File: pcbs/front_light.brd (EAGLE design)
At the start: 28 x 35 mm, 13 parts, among them IC1 MC34063AD, J1 22-27-2041-04

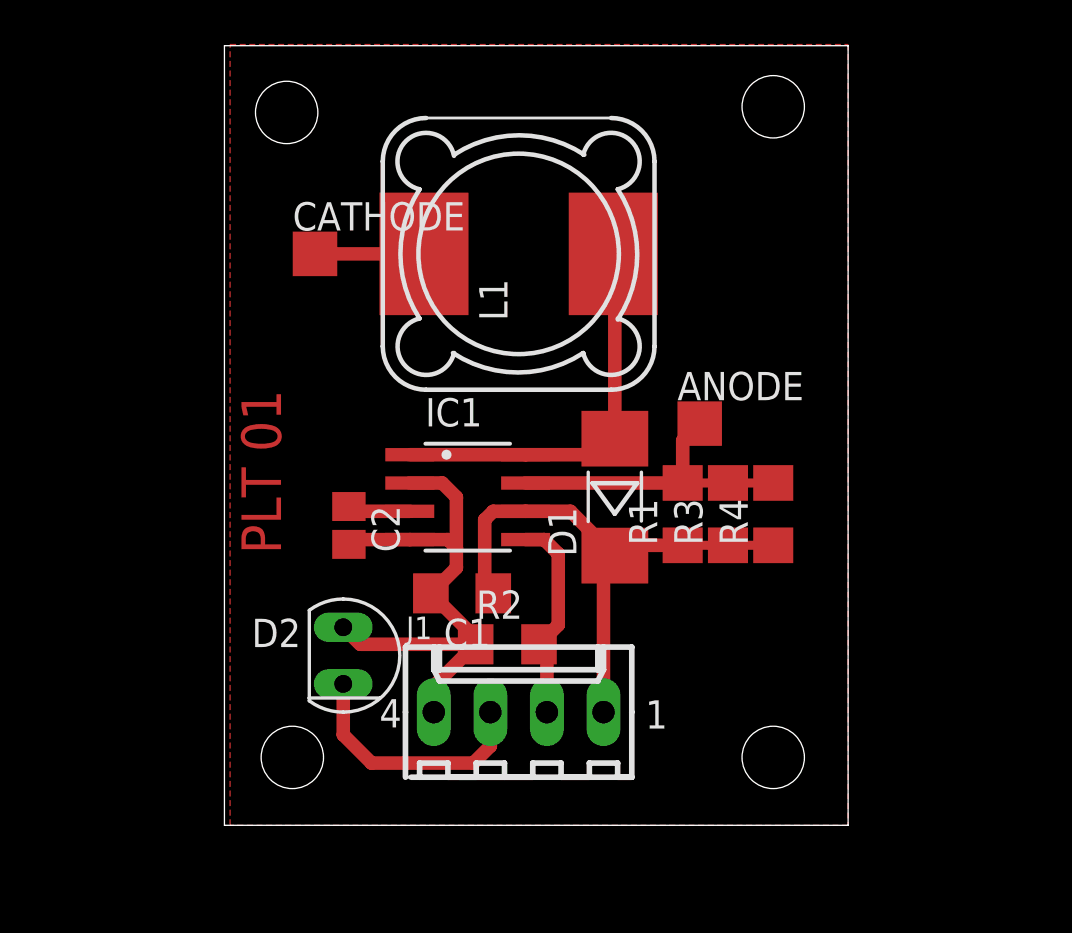
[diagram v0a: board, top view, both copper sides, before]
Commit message: Front light: use attiny and LT3474
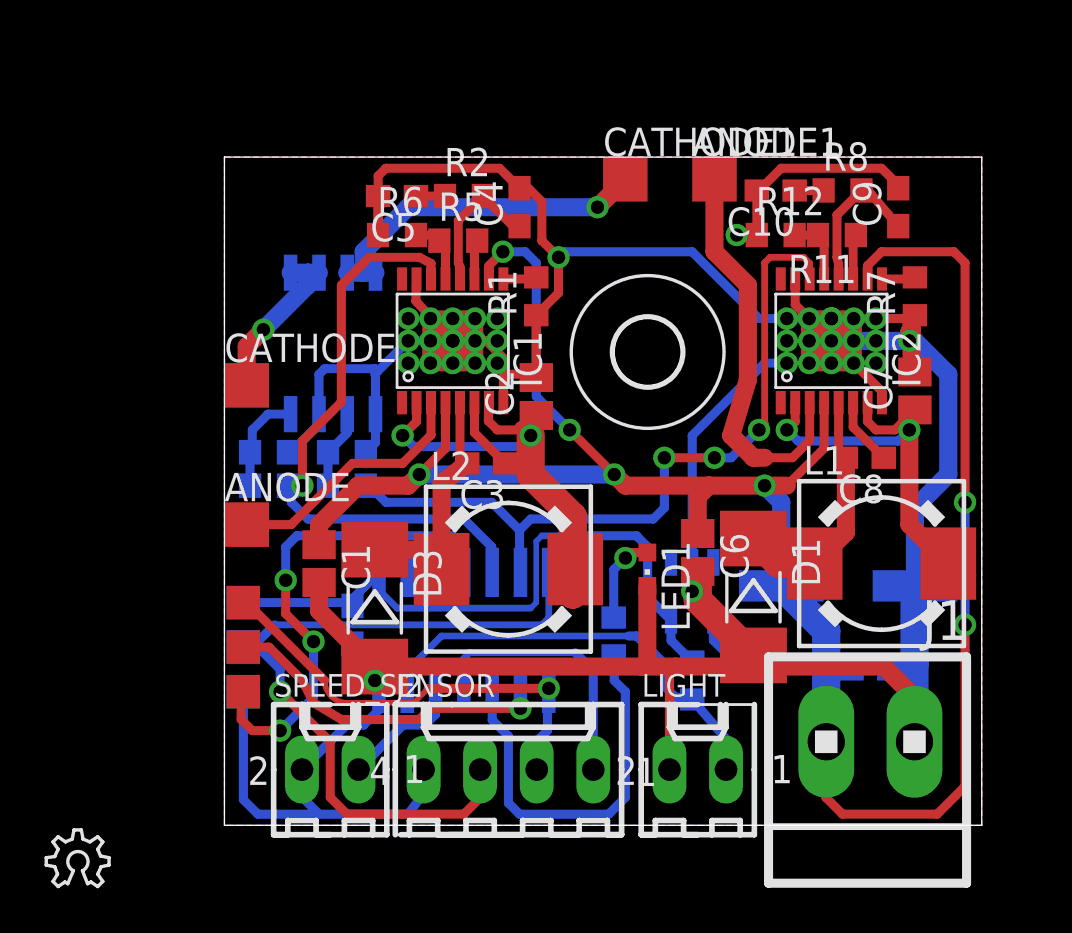
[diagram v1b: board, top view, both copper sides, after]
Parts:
- removed D2: SFH206, opto-trans-siemens:SFH206
- added ANODE1, CATHODE1: TPTP20SQ, testpad:TP20SQ
- added C10, C11, C14, C5: 100n, resistor:C0603
- added C13: 100u, resistor:PANASONIC_E
- added C3, C8: 220n, resistor:C0603
- added C4, C9: 3.3n, resistor:C0603
- added C6, C7: 2.2u, resistor:C0805
- added D3: LL5819, Brunner:MELF-MLL41
- added H1: MOUNT-HOLE3.0, holes:3,0
- added IC2: LT3474, ltc_swr:TSSOP16_BA
- added IC3: ATTINY24/44/84-SSU, attiny24_44_84:SOIC14
- added J2: 22-27-2041-04, con-molex:6410-04
- added L2: DR74, inductors:DR74
- added LED1: (no value), led:CHIPLED_0603
- added LIGHT, SPEED_SENSOR: 22-27-2021-02, con-molex:6410-02
- added LOGO1: OSHW_LOGO_6MILX0100-NT, ea:OSHW_6X100_NOTEXT
- added R10: 100k, resistor:R0603
- added R11, R5: 10k, resistor:R0603
- added R12, R6: 20k, resistor:R0603
- added R13, R14: (no value), resistor:R0603
- added R7, R8: 52.3k, resistor:R0603
- added R9: 33, resistor:R0603
- added U$1: TPS71530, ShortCircuitRobotics:SOT23-DBV
- added U$2: ISP_SPECIALS, bookla:ISP_RM2_00_STRAIGHT
- added U$4: IRF7103, irf-2:SO8-2
- C1: value 10u -> 2.2u; device resistor:C1206 -> resistor:C0805
- C2: value 330p -> 2.2u
- IC1: value MC34063AD -> LT3474; device v-reg-3:SO08 -> ltc_swr:TSSOP16_BA
- J1: value 22-27-2041-04 -> (none); device con-molex:6410-04 -> con-amp:1X2MTA
- L1: value 470u -> DR74; device inductor-coilcraft:MSS1260 -> inductors:DR74
- R1: value 1R0 -> 52.3k; device rcl:R1206 -> resistor:R0603
- R2: value (none) -> 52.3k; device resistor:R1206 -> resistor:R0603
- R3: value 1R0 -> 33; device rcl:R1206 -> resistor:R0603
- R4: value 1R0 -> 100k; device rcl:R1206 -> resistor:R0603
- moved R4 22.8 mm to (2.00, 16.8), flipped to the bottom, turned to 0 degrees
- moved L1 21.4 mm to (29.5, 11.8), turned to 0 degrees
- moved ANODE 20.8 mm to (1.00, 13.5)
- moved R3 20.6 mm to (2.00, 15.2), flipped to the bottom, turned to 0 degrees
- moved R2 20.2 mm to (10.8, 28.2)
- moved J1 15.8 mm to (29.0, 3.75), turned to 180 degrees
- moved R1 11.8 mm to (14.0, 23.8)
- moved C2 10.2 mm to (14.0, 19.2), turned to 90 degrees
- moved D1 7.67 mm to (23.8, 10.2), turned to 270 degrees
- moved IC1 7.05 mm to (10.2, 21.8), turned to 0 degrees
- moved CATHODE 6.65 mm to (1.00, 19.8)
- moved C1 6.56 mm to (4.25, 11.8), turned to 270 degrees
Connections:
- removed net LED_A: ANODE.TP, IC1.7, R1.2, R3.2, R4.2
- removed net LED_C: CATHODE.TP, L1.P$1
- removed net LIGHT: D2.K, J1.3
- removed net PWM: IC1.5, J1.2, R2.2
- new net +12V: C1.1, C11.1, C13.+, C6.1, IC1.10, IC1.4, IC2.10, IC2.4, J1.1, U$1.4
- new net DI: IC3.7, J2.3, U$2.MOSI
- new net DO: IC3.8, J2.2, U$2.RESET
- new net N$10: R3.2, R4.2, U$4.4
- new net N$11: IC1.13, R5.1, R6.2
- new net N$12: C8.2, D1.C, IC2.5, L1.1
- new net N$13: C7.1, IC2.2, IC2.7, L1.2
- new net N$14: IC2.9, R7.2
- new net N$15: IC2.11, R11.1
- new net N$16: C8.1, IC2.6
- new net N$17: C9.1, IC2.12, R8.2
- new net N$18: C10.1, R8.1
- new net N$19: ANODE1.TP, IC2.3
- new net N$2: C2.1, IC1.2, IC1.7, L2.2
- new net N$20: CATHODE1.TP, U$4.7, U$4.8
- new net N$21: R10.2, R9.2, U$4.2
- new net N$22: IC2.13, R11.2, R12.2
- new net N$23: IC3.9, U$2.SCK
- new net N$24: IC3.13, LIGHT.1, R14.1
- new net N$25: IC3.10, R13.1
- new net N$26: LED1.A, R13.2
- new net N$27: IC3.12, SPEED_SENSOR.1
- new net N$3: IC1.11, R5.2
- new net N$4: IC1.9, R1.2
- new net N$5: C3.1, IC1.6
- new net N$6: C4.1, IC1.12, R2.2
- new net N$8: ANODE.TP, IC1.3
- new net N$9: CATHODE.TP, U$4.5, U$4.6
- new net PWM_BIG_LED: IC2.14, IC3.6, R9.1
- new net PWM_DLR: IC1.14, IC3.5, R3.1
- new net RESET: IC3.4, U$2.MISO
- new net WAKE_UP: IC3.11, J2.1
- net GND: now also C10.2, C11.2, C13.-, C14.2, C4.2, C5.2, C6.2, C7.2, C9.2, D1.A, D3.A, IC1.15, IC1.8, IC1.EXP, IC2.15, IC2.8, IC2.EXP, IC3.14, J1.2, J2.4, LED1.C, LIGHT.2, R1.1, R10.1, R12.1, R4.1, R6.1, R7.1, SPEED_SENSOR.2, U$1.2, U$2.VCC, U$4.1, U$4.3; no longer D2.A, IC1.2, IC1.4, J1.4, R2.1
- net N$1: now also C3.2, D3.C, IC1.5, L2.1; no longer D1.A, IC1.1, IC1.8, L1.P$2
- net N$7: now also C5.1, R2.1; no longer C2.1, IC1.3
- net VCC: now also C14.1, IC3.1, R14.2, U$1.5, U$2.GND; no longer C1.1, D1.C, IC1.6, J1.1, R1.1, R3.1, R4.1
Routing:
- net GND: track 25.4 -> 200.2 mm, vias 0 -> 37
- net +12V: track 0.00 -> 108.0 mm, vias 0 -> 7
- net PWM_BIG_LED: track 0.00 -> 34.1 mm, vias 0 -> 3
- net DI: track 0.00 -> 33.2 mm, vias 0 -> 1
- net PWM_DLR: track 0.00 -> 27.5 mm, vias 0 -> 1
- net RESET: track 0.00 -> 22.2 mm, vias 0 -> 3
- net N$2: track 0.00 -> 21.6 mm, vias 0 -> 2
- net DO: track 0.00 -> 20.1 mm, vias 0 -> 1
- net N$24: track 0.00 -> 19.7 mm
- net N$13: track 0.00 -> 18.5 mm, vias 0 -> 2
- net N$19: track 0.00 -> 18.2 mm
- net N$25: track 0.00 -> 17.8 mm
- net N$20: track 0.00 -> 15.3 mm, vias 0 -> 1
- net N$23: track 0.00 -> 15.0 mm, vias 0 -> 1
- net LED_A: track 14.1 -> 0.00 mm
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- added copper zone on layer 16, net GND
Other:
- board size 28 x 35 mm -> 34 x 30 mm
- board text removed: "PLT 01"

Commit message: ForntLight: improved silkscreen
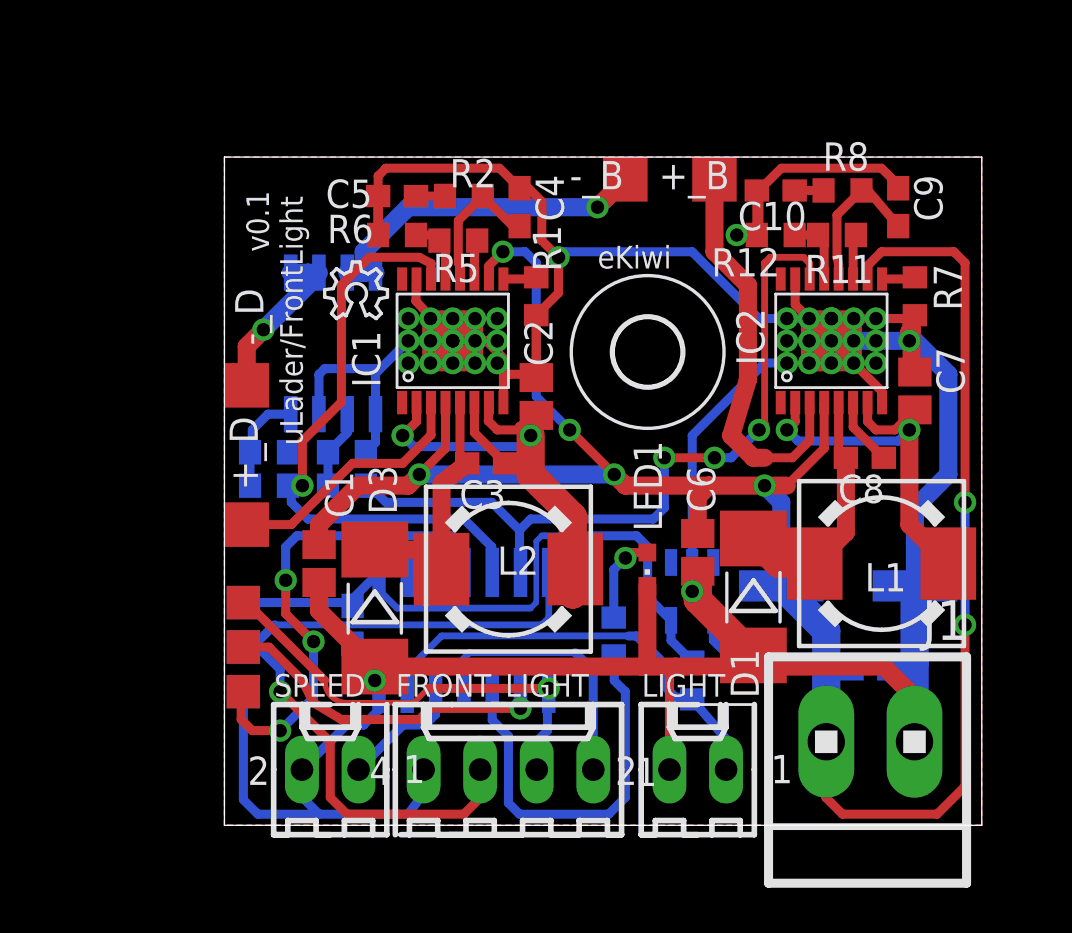
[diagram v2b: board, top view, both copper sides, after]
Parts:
- added LOGO2: OSHW_LOGO_10MILX0350-NT, ea:OSHW_10X350_NOTEXT
- moved LOGO1 28.4 mm to (4.50, 22.8)
- renumbered ANODE to +_D, ANODE1 to +_B, CATHODE to -_D, CATHODE1 to -_B, J2 to FRONT_LIGHT, SPEED_SENSOR to SPEED, U$4 to IRF7103
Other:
- board text added: "eKiwi"
- board text added: "https://github.com/ekiwi/ulader"
- board text added: "https://github.com/roboterclubaachen/xpcc"
- board text added: "uLader/FrontLight"
- board text added: "v0.1"

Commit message: FrontLight: solved some DRC errors
If the .dru file from OSH Park is used
and clearance od same signal smd, pad and via
is set to 0, we do not get any DRC errors.
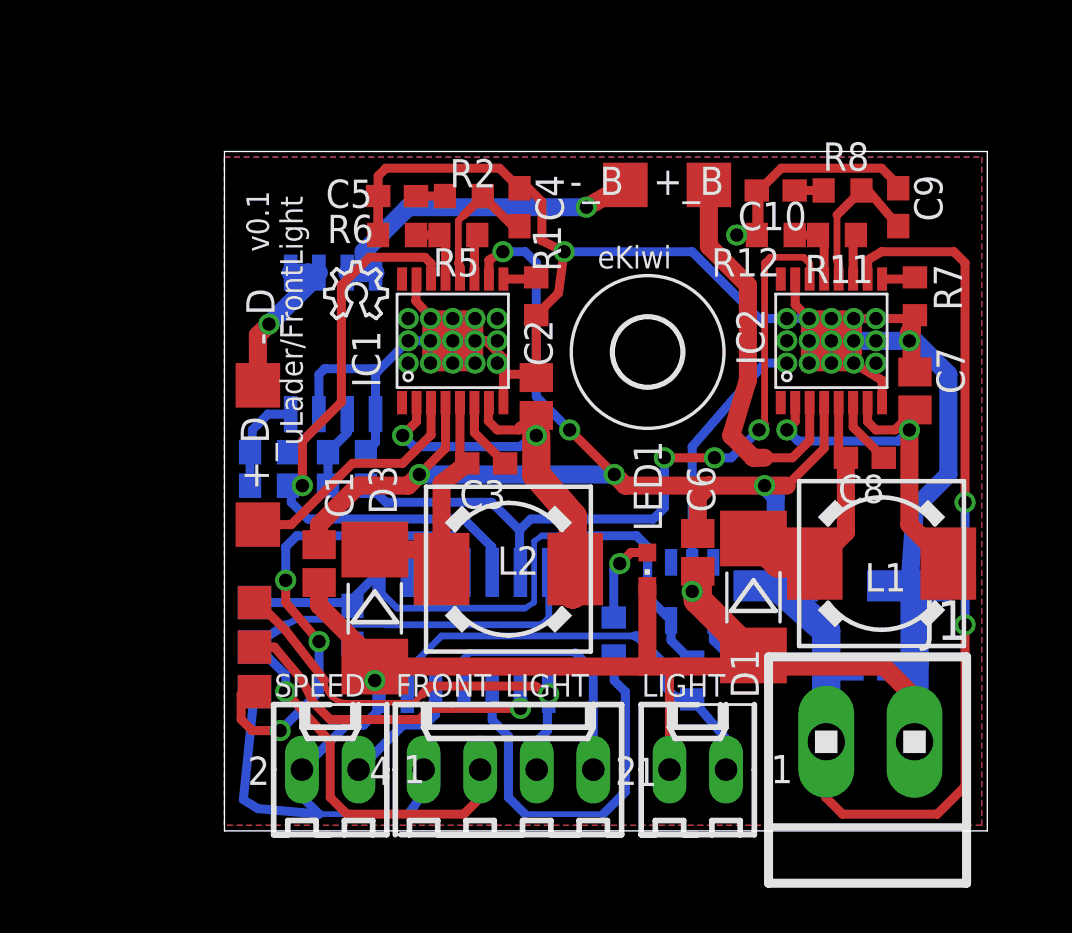
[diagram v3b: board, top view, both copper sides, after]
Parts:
- moved +_D 0.50 mm to (1.50, 13.5)
- moved -_D 0.50 mm to (1.50, 19.8)
- moved U$2 0.50 mm to (0.50, 8.00)
- moved +_B 0.35 mm to (21.8, 28.8)
- moved -_B 0.25 mm to (18.0, 28.8)
- moved C13 0.25 mm to (27.8, 10.8)
- moved R5 0.25 mm to (10.5, 26.5)
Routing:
- net RESET: track 22.2 -> 22.8 mm
- net DO: track 20.1 -> 20.7 mm
- net VCC: track 29.3 -> 28.7 mm
- net N$8: track 11.4 -> 10.9 mm
- net GND: track 200.2 -> 200.4 mm, vias 37 -> 35
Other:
- board size 34 x 30 mm -> 34.2 x 30.5 mm

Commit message: FrontLight: use only one LT3474
Since the DLR and the big led will never be used
together they can be driven by a single
led constant current switching IC.
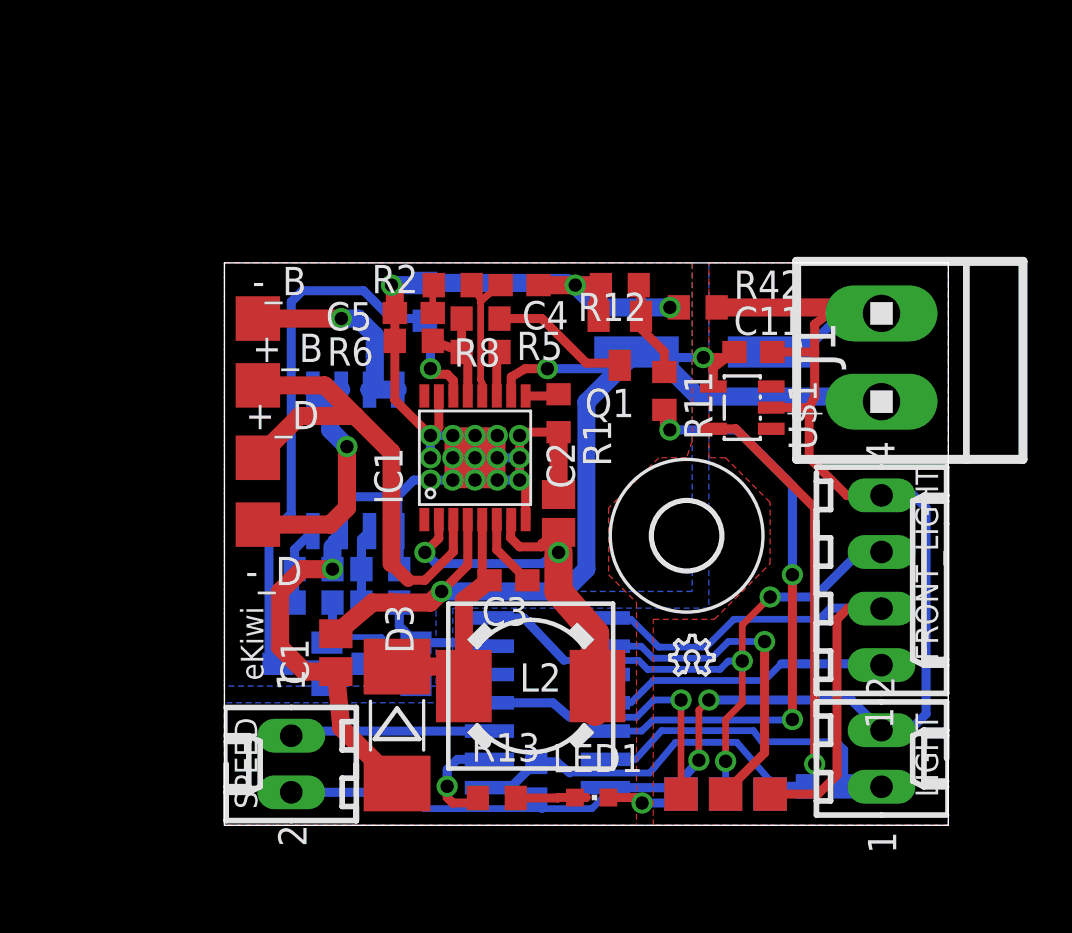
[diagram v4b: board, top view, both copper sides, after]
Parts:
- removed C10: 100n, resistor:C0603
- removed C6, C7: 2.2u, resistor:C0805
- removed C8: 220n, resistor:C0603
- removed C9: 3.3n, resistor:C0603
- removed IC2: LT3474, ltc_swr:TSSOP16_BA
- removed L1: DR74, inductors:DR74
- removed LOGO2: OSHW_LOGO_10MILX0350-NT, ea:OSHW_10X350_NOTEXT
- added D2: BAT54, diode:SOT23
- added Q1: BSS123, transistor-small-signal:SOT23
- added R42: 0, rcl:R0603
- D1: value LL5819 -> BAT54; device Brunner:MELF-MLL41 -> diode:SOT23
- LOGO1: value OSHW_LOGO_6MILX0100-NT -> OSHW_LOGO_6MILX0070-NT; device ea:OSHW_6X100_NOTEXT -> ea:OSHW_6X70_NOTEXT
- R11: value 10k -> 33
- R12: value 20k -> 100k
- R5: value 10k -> 100k
- R6: value 20k -> 200k
- R8: value 52.3k -> 1
- moved U$2 22.7 mm to (22.5, 2.25), turned to 0 degrees
- moved LOGO1 22.3 mm to (20.0, 6.75)
- moved +_B 22.2 mm to (1.50, 19.8)
- moved R7 22.0 mm to (9.00, 23.5), flipped to the bottom
- moved D1 20.5 mm to (3.50, 7.25), flipped to the bottom
- moved FRONT_LIGHT 18.8 mm to (29.5, 11.0), turned to 270 degrees
- moved -_B 17.6 mm to (1.50, 22.8)
- moved J1 17.3 mm to (29.5, 21.0), turned to 270 degrees
- moved R8 17.2 mm to (11.5, 22.8), turned to 180 degrees
- moved C11 15.2 mm to (23.8, 21.2), flipped to the top, turned to 0 degrees
- moved C13 12.2 mm to (21.5, 21.2)
- moved C14 10.8 mm to (14.0, 2.00)
- moved LED1 10.6 mm to (16.5, 1.25), turned to 270 degrees
- moved R11 10.4 mm to (19.8, 19.5), turned to 270 degrees
- moved R13 8.95 mm to (12.2, 1.23), flipped to the top, turned to 0 degrees
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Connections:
- removed net N$14: IC2.9, R7.2
- removed net N$16: C8.1, IC2.6
- removed net N$17: C9.1, IC2.12, R8.2
- removed net N$18: C10.1, R8.1
- removed net N$19: +_B.TP, IC2.3
- removed net N$22: IC2.13, R11.2, R12.2
- removed net N$27: IC3.12, SPEED.1
- new net DLR_ON: IC3.12, R11.2
- new net GNDA: C1.2, C2.2, C4.2, C5.2, D3.A, IC1.15, IC1.8, IC1.EXP, IRF7103.1, IRF7103.3, Q1.2, R1.1, R10.1, R12.1, R4.1, R42.1, R6.1, R7.2
- new net PWM: D1.3, D2.3, IC1.14, R7.1
- net +12V: no longer C6.1, IC2.10, IC2.4
- net GND: now also R42.2; no longer C1.2, C10.2, C2.2, C4.2, C5.2, C6.2, C7.2, C9.2, D1.A, D3.A, IC1.15, IC1.8, IC1.EXP, IC2.15, IC2.8, IC2.EXP, IRF7103.1, IRF7103.3, R1.1, R10.1, R12.1, R4.1, R6.1, R7.1
- net N$11: now also R8.2
- net N$12: now also IC3.3, SPEED.1; no longer C8.2, D1.C, IC2.5, L1.1
- net N$13: now also Q1.3, R8.1; no longer C7.1, IC2.2, IC2.7, L1.2
- net N$15: now also Q1.1, R12.2; no longer IC2.11
- net N$25: now also IC3.2; no longer IC3.10
- net N$8: now also +_B.TP
- net PWM_BIG_LED: now also D2.1; no longer IC2.14
- net PWM_DLR: now also D1.1; no longer IC1.14
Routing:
- net GND: track 200.4 -> 78.8 mm, vias 35 -> 3
- net GNDA: track 0.00 -> 78.4 mm, vias 0 -> 19
- net +12V: track 108.3 -> 53.9 mm, vias 7 -> 3
- net PWM: track 0.00 -> 34.7 mm, vias 0 -> 1
- net PWM_BIG_LED: track 34.1 -> 5.47 mm, vias 3 -> 0
- net DLR_ON: track 0.00 -> 26.6 mm, vias 0 -> 3
- net N$19: track 18.0 -> 0.00 mm
- net PWM_DLR: track 27.5 -> 9.94 mm, vias 1 -> 0
- net N$25: track 17.5 -> 4.91 mm, vias 0 -> 1
- net N$13: track 18.5 -> 6.26 mm, vias 2 -> 0
- net N$8: track 10.9 -> 22.5 mm
- net RESET: track 22.8 -> 13.4 mm, vias 3 -> 1
- net VCC: track 28.7 -> 35.8 mm, vias 0 -> 1
- net N$17: track 6.83 -> 0.00 mm
- net DO: track 20.7 -> 27.2 mm, vias 1 -> 0
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- added copper zone on layer 1, net GNDA
- added copper zone on layer 16, net GNDA
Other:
- board size 34.2 x 30.5 mm -> 32.5 x 25.2 mm
- board text added: "https://github.com/ ekiwi/ulader"
- board text added: "powered by XPCC"
- board text added: "uLader / FrontLight v0.1"
- board text removed: "https://github.com/ekiwi/ulader"
- board text removed: "https://github.com/roboterclubaachen/xpcc"
- board text removed: "uLader/FrontLight"
- board text removed: "v0.1"
